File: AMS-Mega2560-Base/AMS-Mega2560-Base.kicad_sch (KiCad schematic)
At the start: 22 parts, among them J1 RTD1, J2 RTD2, J3 Conn_01x08, J4 Sense1, J5 Sense2, J6 AdafruitUltimateGPS, J7 Conn_02x03_Odd_Even, P1 Power, P10 CONN_01X01, P11 CONN_01X01, P12 CONN_01X01, P13 CONN_01X01, P2 Analog, P3 Analog, P4 Digital, P5 PWM, P6 PWM, P7 Communication, P8 CONN_01X01, P9 CONN_01X01

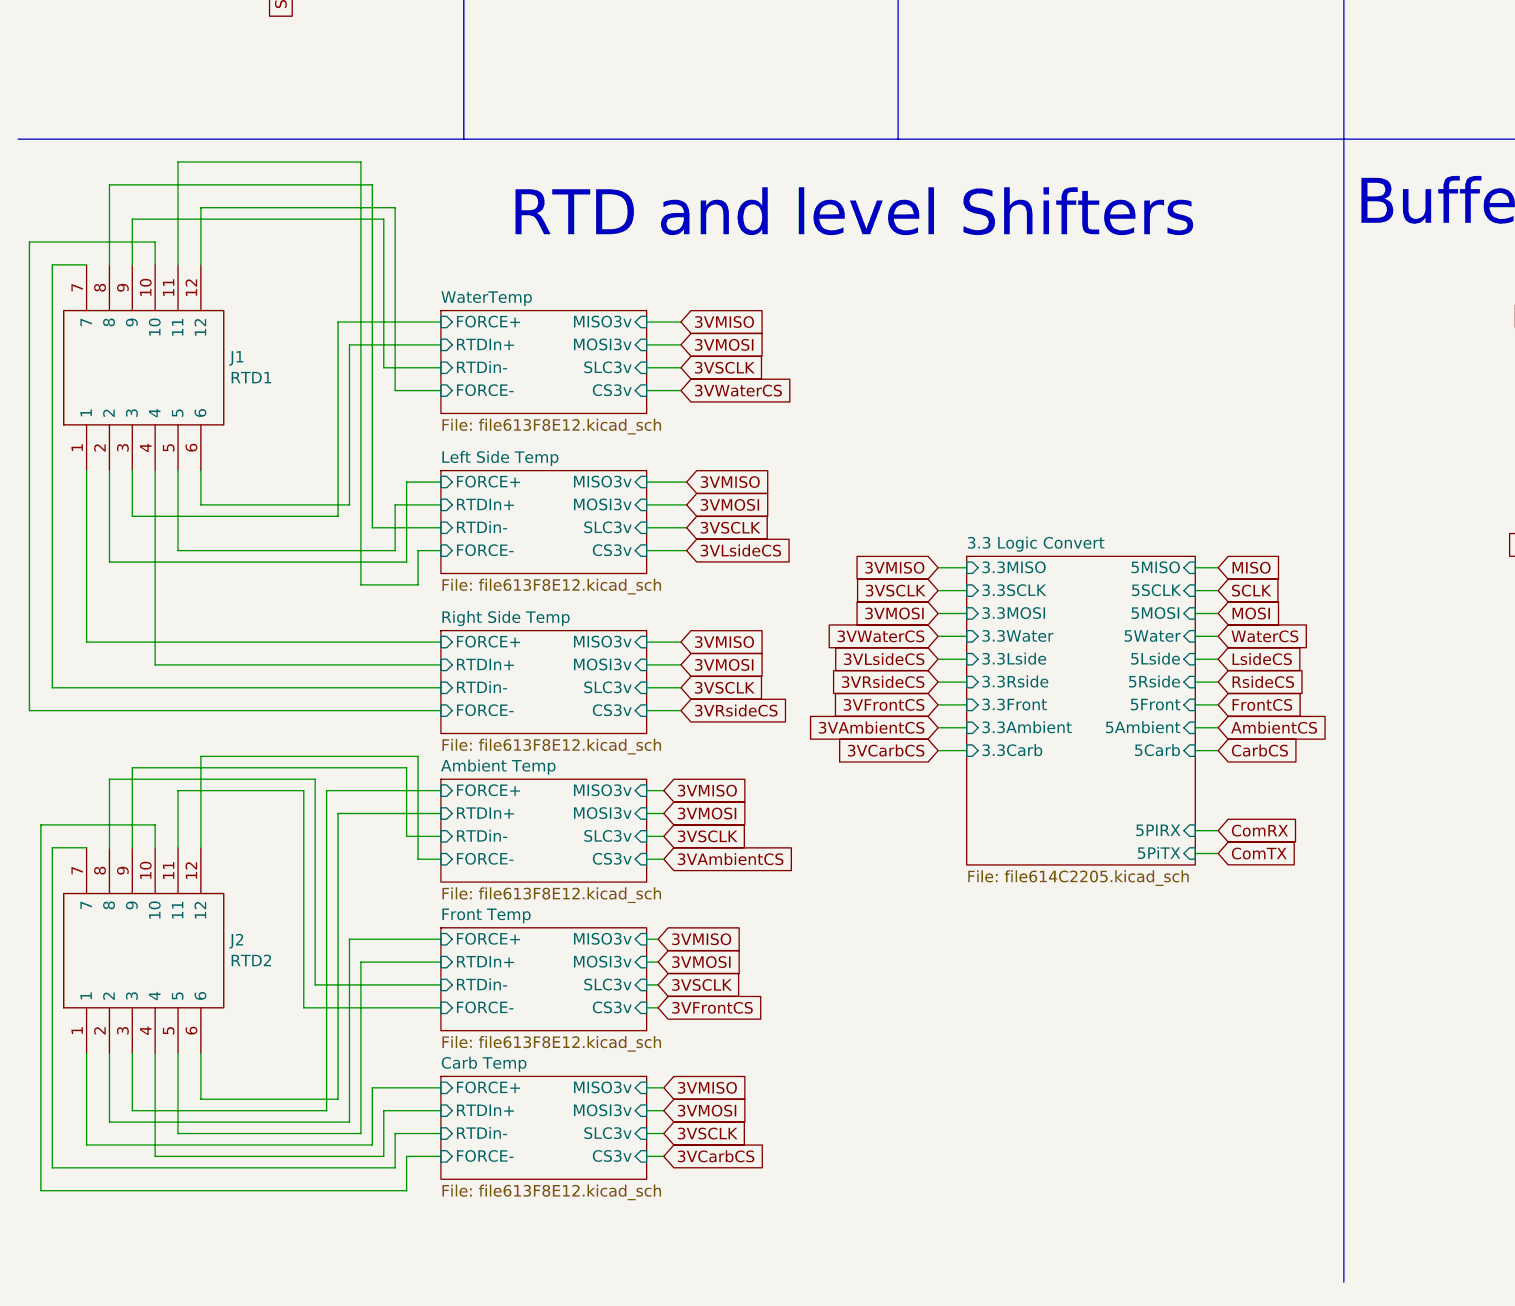
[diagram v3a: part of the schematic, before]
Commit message: removing separate project for lack of chips and switching to dev boards. copied out the schematics used.
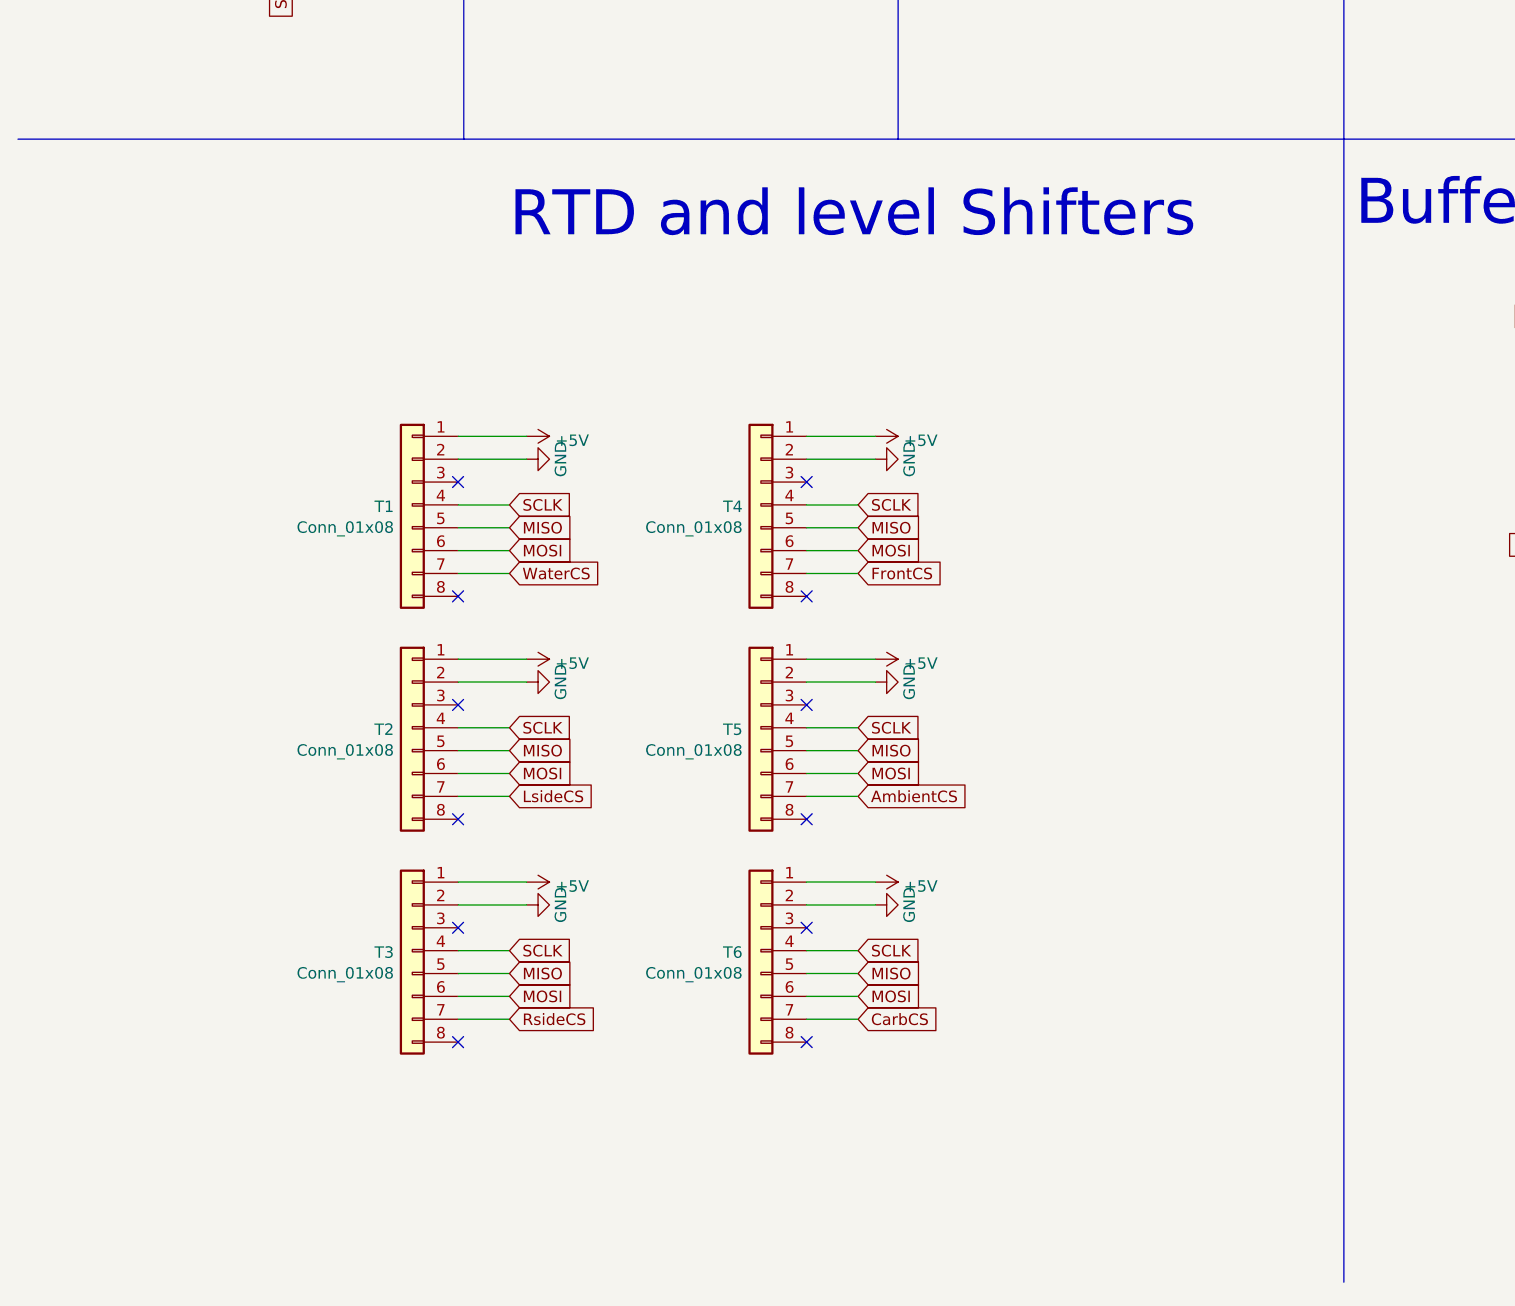
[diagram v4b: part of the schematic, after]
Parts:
- removed J1: RTD1, SamacSys_Parts:1727751, symbol SamacSys_Parts:1727751
- removed J2: RTD2, SamacSys_Parts:1727751, symbol SamacSys_Parts:1727751
- added T1, T2, T3, T4, T5, T6: Conn_01x08, Connector_PinSocket_2.54mm:PinSocket_1x08_P2.54mm_Vertical, symbol Connector_Generic:Conn_01x08
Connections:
- net +5V: now also T1.1 (Pin_1), T2.1 (Pin_1), T3.1 (Pin_1), T4.1 (Pin_1), T5.1 (Pin_1), T6.1 (Pin_1)
- net AmbientCS: now also T5.7 (Pin_7)
- net CarbCS: now also T6.7 (Pin_7)
- net FrontCS: now also T4.7 (Pin_7)
- net GND: now also T1.2 (Pin_2), T2.2 (Pin_2), T3.2 (Pin_2), T4.2 (Pin_2), T5.2 (Pin_2), T6.2 (Pin_2)
- net LsideCS: now also T2.7 (Pin_7)
- net MISO: now also T1.5 (Pin_5), T2.5 (Pin_5), T3.5 (Pin_5), T4.5 (Pin_5), T5.5 (Pin_5), T6.5 (Pin_5)
- net MOSI: now also T1.6 (Pin_6), T2.6 (Pin_6), T3.6 (Pin_6), T4.6 (Pin_6), T5.6 (Pin_6), T6.6 (Pin_6)
- net RsideCS: now also T3.7 (Pin_7)
- net SCLK: now also T1.4 (Pin_4), T2.4 (Pin_4), T3.4 (Pin_4), T4.4 (Pin_4), T5.4 (Pin_4), T6.4 (Pin_4)
- net WaterCS: now also T1.7 (Pin_7)
- no-connect marks 47 -> 59
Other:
- removed sheet 3.3 Logic Convert
- removed sheet Ambient Temp
- removed sheet Carb Temp
- removed sheet Front Temp
- removed sheet Left Side Temp
- removed sheet Right Side Temp
- removed sheet WaterTemp

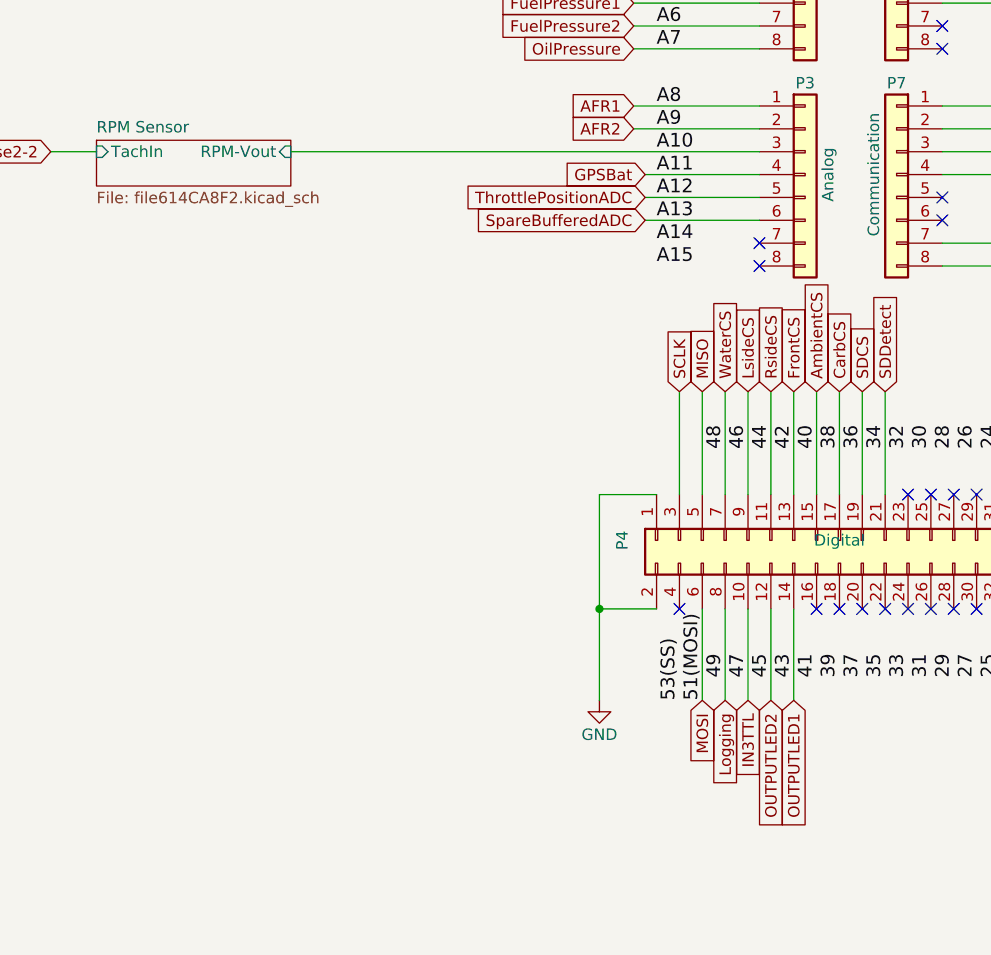
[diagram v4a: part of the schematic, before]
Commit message: applying some fixes for the RPM sensor and other parts of the schem
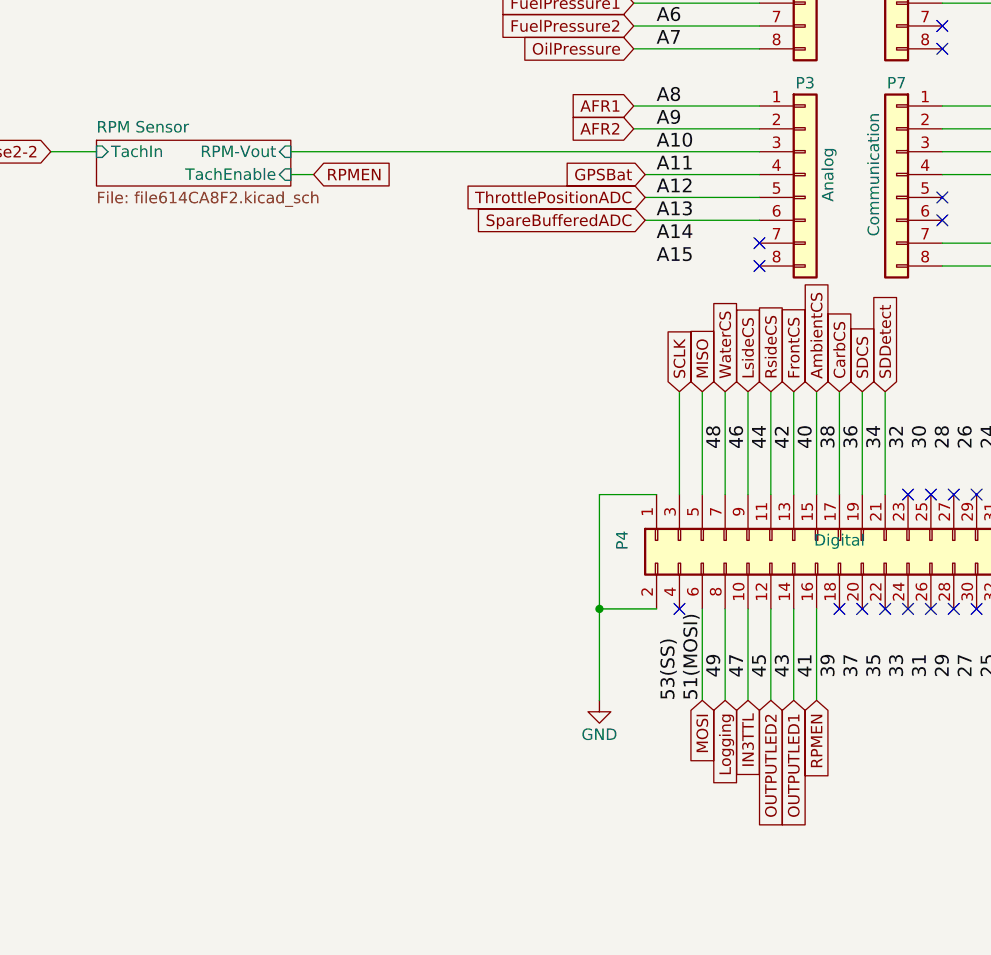
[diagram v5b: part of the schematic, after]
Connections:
- net RPMEN: now reaches P4.16 (Pin_16)
- no-connect marks 59 -> 58
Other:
- sheet RPM Sensor ports: added TachEnable; removed none
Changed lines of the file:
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@@
   (no_connect (at 382.27 142.24))
   (no_connect (at 384.81 142.24))
-  (no_connect (at 361.95 142.24))
   (no_connect (at 377.19 142.24))
   (no_connect (at 379.73 142.24))
@@
     (stroke (width 0) (type default) (color 0 0 0 0))
   )
+  (wire (pts (xy 303.53 93.98) (xy 306.07 93.98))
+    (stroke (width 0) (type default) (color 0 0 0 0))
+  )
   (wire (pts (xy 341.63 62.23) (xy 355.6 62.23))
     (stroke (width 0) (type default) (color 0 0 0 0))
@@
     (stroke (width 0) (type default) (color 0 0 0 0))
   )
+  (wire (pts (xy 361.95 142.24) (xy 361.95 152.4))
+    (stroke (width 0) (type default) (color 0 0 0 0))
+  )
   (polyline (pts (xy 160.02 157.48) (xy 160.02 284.48))
     (stroke (width 0) (type default) (color 0 0 0 0))
@@
     )
   )
+  (global_label "RPMEN" (shape input) (at 306.07 93.98 0) (fields_autoplaced)
+    (effects (font (size 1.27 1.27)) (justify left))
+    (property "Intersheet References" "${INTERSHEET_REFS}" (id 0) (at 314.8652 94.0594 0)
+      (effects (font (size 1.27 1.27)) (justify left) hide)
+    )
+  )
   (global_label "Vacuum2" (shape input) (at 341.63 69.85 180) (fields_autoplaced)
     (effects (font (size 1.27 1.27)) (justify right))
@@
     )
   )
+  (global_label "RPMEN" (shape input) (at 361.95 152.4 270) (fields_autoplaced)
+    (effects (font (size 1.27 1.27)) (justify right))
+    (property "Intersheet References" "${INTERSHEET_REFS}" (id 0) (at 361.8706 161.1952 90)
+      (effects (font (size 1.27 1.27)) (justify right) hide)
+    )
+  )
   (global_label "Sense1-10" (shape input) (at 190.5 177.165 180) (fields_autoplaced)
     (effects (font (size 1.27 1.27)) (justify right))
@@
       (effects (font (size 1.27 1.27)) (justify left))
     )
+    (pin "TachEnable" input (at 303.53 93.98 0)
+      (effects (font (size 1.27 1.27)) (justify right))
+    )
   )
   (sheet (at 276.86 58.42) (size 26.67 12.7) (fields_autoplaced)
@@
       (reference "#PWR037") (unit 1) (value "GND") (footprint "")
     )
-    (path "/00000000-0000-0000-0000-0000614ca8f3/c34d4cb0-d31c-4383-be48-b22a202835b7"
-      (reference "#PWR038") (unit 1) (value "+5V") (footprint "")
-    )
     (path "/00000000-0000-0000-0000-0000614ca8f3/1c3dd39a-24ae-4528-a3a0-5c5eb68aff69"
       (reference "#PWR039") (unit 1) (value "GND") (footprint "")
@@
       (reference "#PWR0144") (unit 1) (value "GND") (footprint "")
     )
+    (path "/00000000-0000-0000-0000-0000623d3962/e124ca3f-ce06-4b28-895a-df0157887c78"
+      (reference "C1") (unit 1) (value "22nF") (footprint "Capacitor_THT:C_Disc_D4.7mm_W2.5mm_P5.00mm")
+    )
+    (path "/00000000-0000-0000-0000-0000623d3962/c626e370-a5ce-47bd-b258-516265b4ca6f"
+      (reference "C2") (unit 1) (value "22nF") (footprint "Capacitor_THT:C_Disc_D4.7mm_W2.5mm_P5.00mm")
+    )
+    (path "/00000000-0000-0000-0000-0000623d3962/ef7c2956-1db8-47e9-88e3-2a0eab74ba7b"
+      (reference "C3") (unit 1) (value "22nF") (footprint "Capacitor_THT:C_Disc_D4.7mm_W2.5mm_P5.00mm")
+    )
+    (path "/00000000-0000-0000-0000-0000623d3962/60e4685d-5e06-4b43-9820-22ec100a23db"
+      (reference "C4") (unit 1) (value "22nF") (footprint "Capacitor_THT:C_Disc_D4.7mm_W2.5mm_P5.00mm")
+    )
     (path "/00000000-0000-0000-0000-000061493c0e/00000000-0000-0000-0000-0000614c526f"
       (reference "C13") (unit 1) (value "15uF") (footprint "Capacitor_THT:CP_Radial_D5.0mm_P2.50mm")
@@
     )
     (path "/00000000-0000-0000-0000-000061493c0e/00000000-0000-0000-0000-0000614ad18b"
-      (reference "C19") (unit 1) (value "C") (footprint "Capacitor_THT:C_Rect_L9.0mm_W3.6mm_P7.50mm_MKT")
+      (reference "C19") (unit 1) (value "3.3nF") (footprint "Capacitor_THT:C_Rect_L9.0mm_W3.6mm_P7.50mm_MKT")
     )
     (path "/00000000-0000-0000-0000-000061493c0e/00000000-0000-0000-0000-0000614ad1af"
@@
     )
     (path "/00000000-0000-0000-0000-0000623d3962/a781b66e-4628-4987-b2c2-1aef3a4e7187"
-      (reference "R5") (unit 1) (value "R") (footprint "Resistor_THT:R_Axial_DIN0207_L6.3mm_D2.5mm_P2.54mm_Vertical")
+      (reference "R5") (unit 1) (value "1M") (footprint "Resistor_THT:R_Axial_DIN0207_L6.3mm_D2.5mm_P2.54mm_Vertical")
     )
     (path "/4fa38cd6-152a-4f14-8b73-29a5177e2f36/0381b35b-f354-47d9-8171-23b2631ffc7a"
@@
     )
     (path "/00000000-0000-0000-0000-0000623d3962/00000000-0000-0000-0000-0000623ffb93"
-      (reference "R8") (unit 1) (value "R") (footprint "Resistor_THT:R_Axial_DIN0207_L6.3mm_D2.5mm_P2.54mm_Vertical")
+      (reference "R8") (unit 1) (value "1M") (footprint "Resistor_THT:R_Axial_DIN0207_L6.3mm_D2.5mm_P2.54mm_Vertical")
     )
     (path "/00000000-0000-0000-0000-0000623d3962/00000000-0000-0000-0000-0000623fcdef"
-      (reference "R9") (unit 1) (value "R") (footprint "Resistor_THT:R_Axial_DIN0207_L6.3mm_D2.5mm_P2.54mm_Vertical")
+      (reference "R9") (unit 1) (value "1M") (footprint "Resistor_THT:R_Axial_DIN0207_L6.3mm_D2.5mm_P2.54mm_Vertical")
     )
     (path "/00000000-0000-0000-0000-0000623d3962/83298769-e504-4924-8f7b-9116f50e3f17"
-      (reference "R10") (unit 1) (value "R") (footprint "Resistor_THT:R_Axial_DIN0207_L6.3mm_D2.5mm_P2.54mm_Vertical")
+      (reference "R10") (unit 1) (value "1M") (footprint "Resistor_THT:R_Axial_DIN0207_L6.3mm_D2.5mm_P2.54mm_Vertical")
     )
     (path "/00000000-0000-0000-0000-0000623d3962/6e92d60e-064b-4563-b0e3-5b956d7c8e7d"
-      (reference "R11") (unit 1) (value "R") (footprint "Resistor_THT:R_Axial_DIN0207_L6.3mm_D2.5mm_P2.54mm_Vertical")
+      (reference "R11") (unit 1) (value "330") (footprint "Resistor_THT:R_Axial_DIN0207_L6.3mm_D2.5mm_P2.54mm_Vertical")
     )
     (path "/00000000-0000-0000-0000-000061493c0e/5d5c8cc3-d3db-48b0-ad1c-0ee8b3935a6f"
@@
     )
     (path "/00000000-0000-0000-0000-0000623d3962/17c02880-df6f-4797-b976-af8c3295fb23"
-      (reference "R13") (unit 1) (value "R") (footprint "Resistor_THT:R_Axial_DIN0207_L6.3mm_D2.5mm_P2.54mm_Vertical")
+      (reference "R13") (unit 1) (value "330") (footprint "Resistor_THT:R_Axial_DIN0207_L6.3mm_D2.5mm_P2.54mm_Vertical")
     )
     (path "/00000000-0000-0000-0000-0000623d3962/0c7e8efa-8cd3-44a9-afac-6a74370f5385"
-      (reference "R14") (unit 1) (value "R") (footprint "Resistor_THT:R_Axial_DIN0207_L6.3mm_D2.5mm_P2.54mm_Vertical")
+      (reference "R14") (unit 1) (value "330") (footprint "Resistor_THT:R_Axial_DIN0207_L6.3mm_D2.5mm_P2.54mm_Vertical")
     )
     (path "/00000000-0000-0000-0000-0000623d3962/00000000-0000-0000-0000-0000623ffb8d"
-      (reference "R15") (unit 1) (value "R") (footprint "Resistor_THT:R_Axial_DIN0207_L6.3mm_D2.5mm_P2.54mm_Vertical")
+      (reference "R15") (unit 1) (value "330") (footprint "Resistor_THT:R_Axial_DIN0207_L6.3mm_D2.5mm_P2.54mm_Vertical")
     )
     (path "/00000000-0000-0000-0000-0000623d3962/3270290c-0fa0-4708-bf39-94c10769bbca"
-      (reference "R16") (unit 1) (value "R") (footprint "Resistor_THT:R_Axial_DIN0207_L6.3mm_D2.5mm_P2.54mm_Vertical")
+      (reference "R16") (unit 1) (value "22k") (footprint "Resistor_THT:R_Axial_DIN0207_L6.3mm_D2.5mm_P2.54mm_Vertical")
     )
     (path "/00000000-0000-0000-0000-0000623d3962/00000000-0000-0000-0000-0000623fcde9"
-      (reference "R17") (unit 1) (value "R") (footprint "Resistor_THT:R_Axial_DIN0207_L6.3mm_D2.5mm_P2.54mm_Vertical")
+      (reference "R17") (unit 1) (value "22k") (footprint "Resistor_THT:R_Axial_DIN0207_L6.3mm_D2.5mm_P2.54mm_Vertical")
     )
     (path "/00000000-0000-0000-0000-0000623d3962/36c614fd-4f66-4a7b-b066-184c2dd95f17"
-      (reference "R18") (unit 1) (value "R") (footprint "Resistor_THT:R_Axial_DIN0207_L6.3mm_D2.5mm_P2.54mm_Vertical")
+      (reference "R18") (unit 1) (value "22k") (footprint "Resistor_THT:R_Axial_DIN0207_L6.3mm_D2.5mm_P2.54mm_Vertical")
     )
     (path "/00000000-0000-0000-0000-0000623d3962/7c646663-d855-46dd-a9cf-0ef27a64e8cf"
-      (reference "R19") (unit 1) (value "R") (footprint "Resistor_THT:R_Axial_DIN0207_L6.3mm_D2.5mm_P2.54mm_Vertical")
+      (reference "R19") (unit 1) (value "22k") (footprint "Resistor_THT:R_Axial_DIN0207_L6.3mm_D2.5mm_P2.54mm_Vertical")
     )
     (path "/00000000-0000-0000-0000-000061493c0e/00000000-0000-0000-0000-00006149b74d"
@@
     )
     (path "/00000000-0000-0000-0000-0000614ca8f3/800b125d-466b-48a6-86fb-b0ab67586b77"
-      (reference "R70") (unit 1) (value "R") (footprint "Resistor_THT:R_Axial_DIN0207_L6.3mm_D2.5mm_P2.54mm_Vertical")
+      (reference "R70") (unit 1) (value "1M") (footprint "Resistor_THT:R_Axial_DIN0207_L6.3mm_D2.5mm_P2.54mm_Vertical")
     )
     (path "/00000000-0000-0000-0000-0000614ca8f3/00000000-0000-0000-0000-0000614e2c3c"
